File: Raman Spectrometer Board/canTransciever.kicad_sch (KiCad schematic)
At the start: 17 parts, among them SW1 SW_Push, SW2 SW_Push, U6 ATA6561, U7 ATA6561

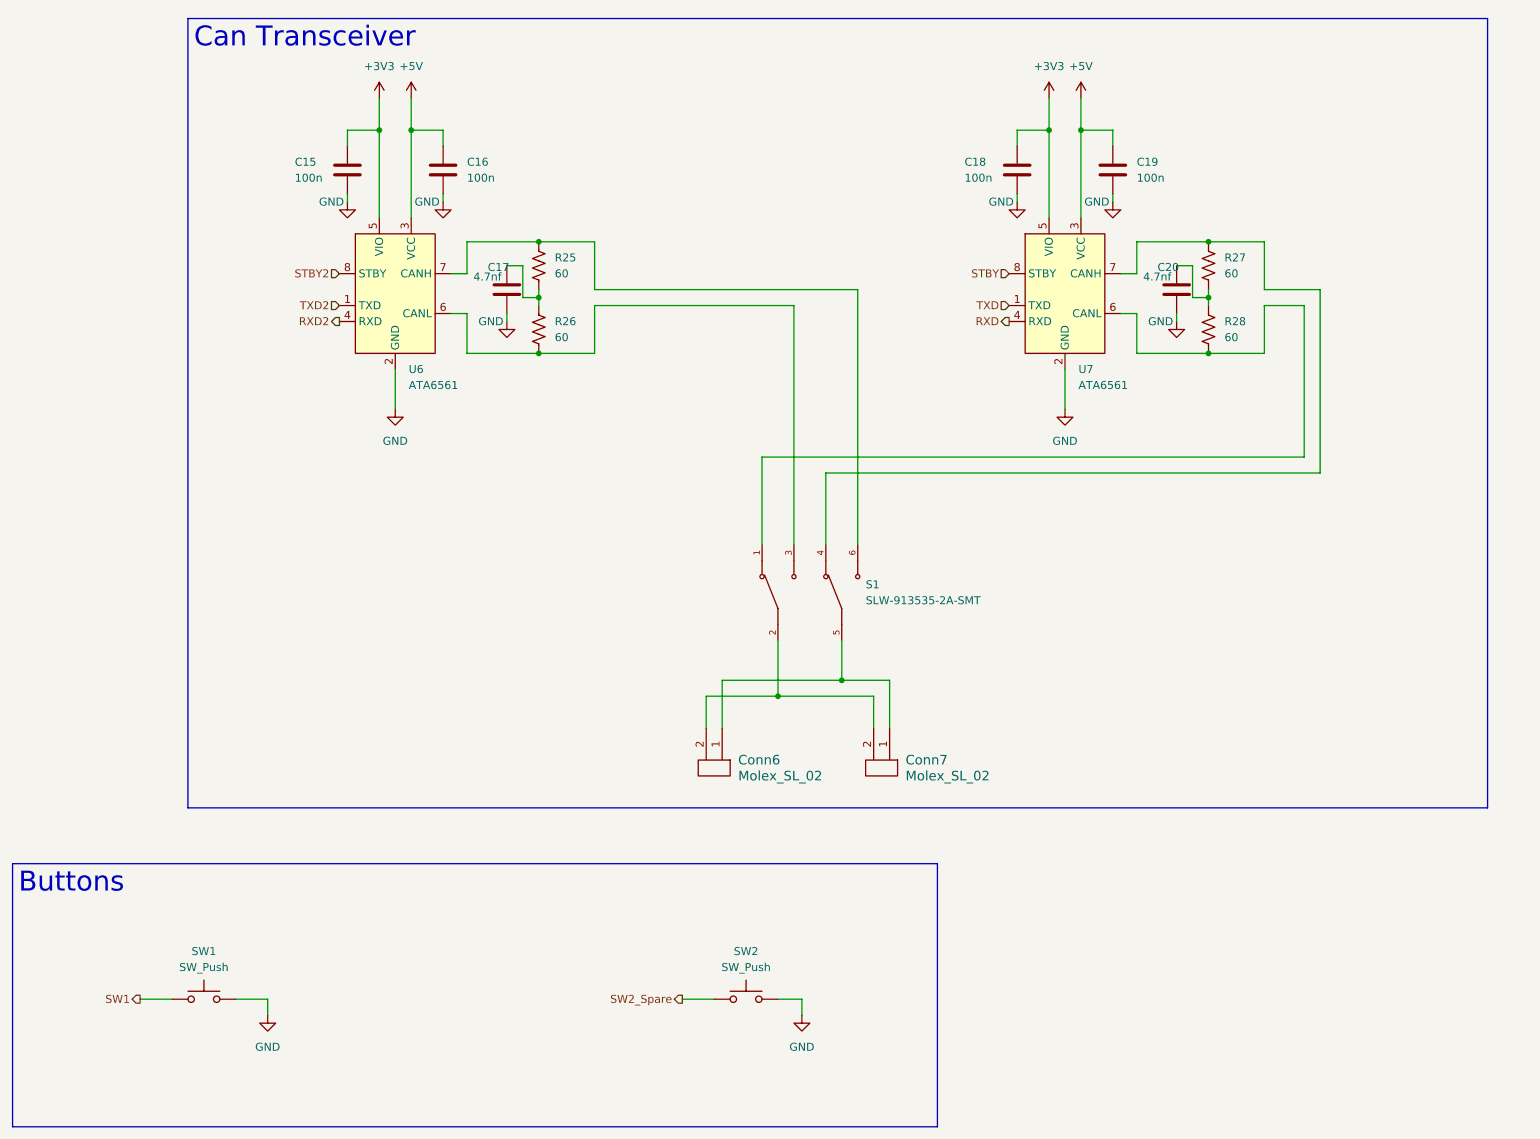
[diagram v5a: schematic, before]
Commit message: SCH fixes
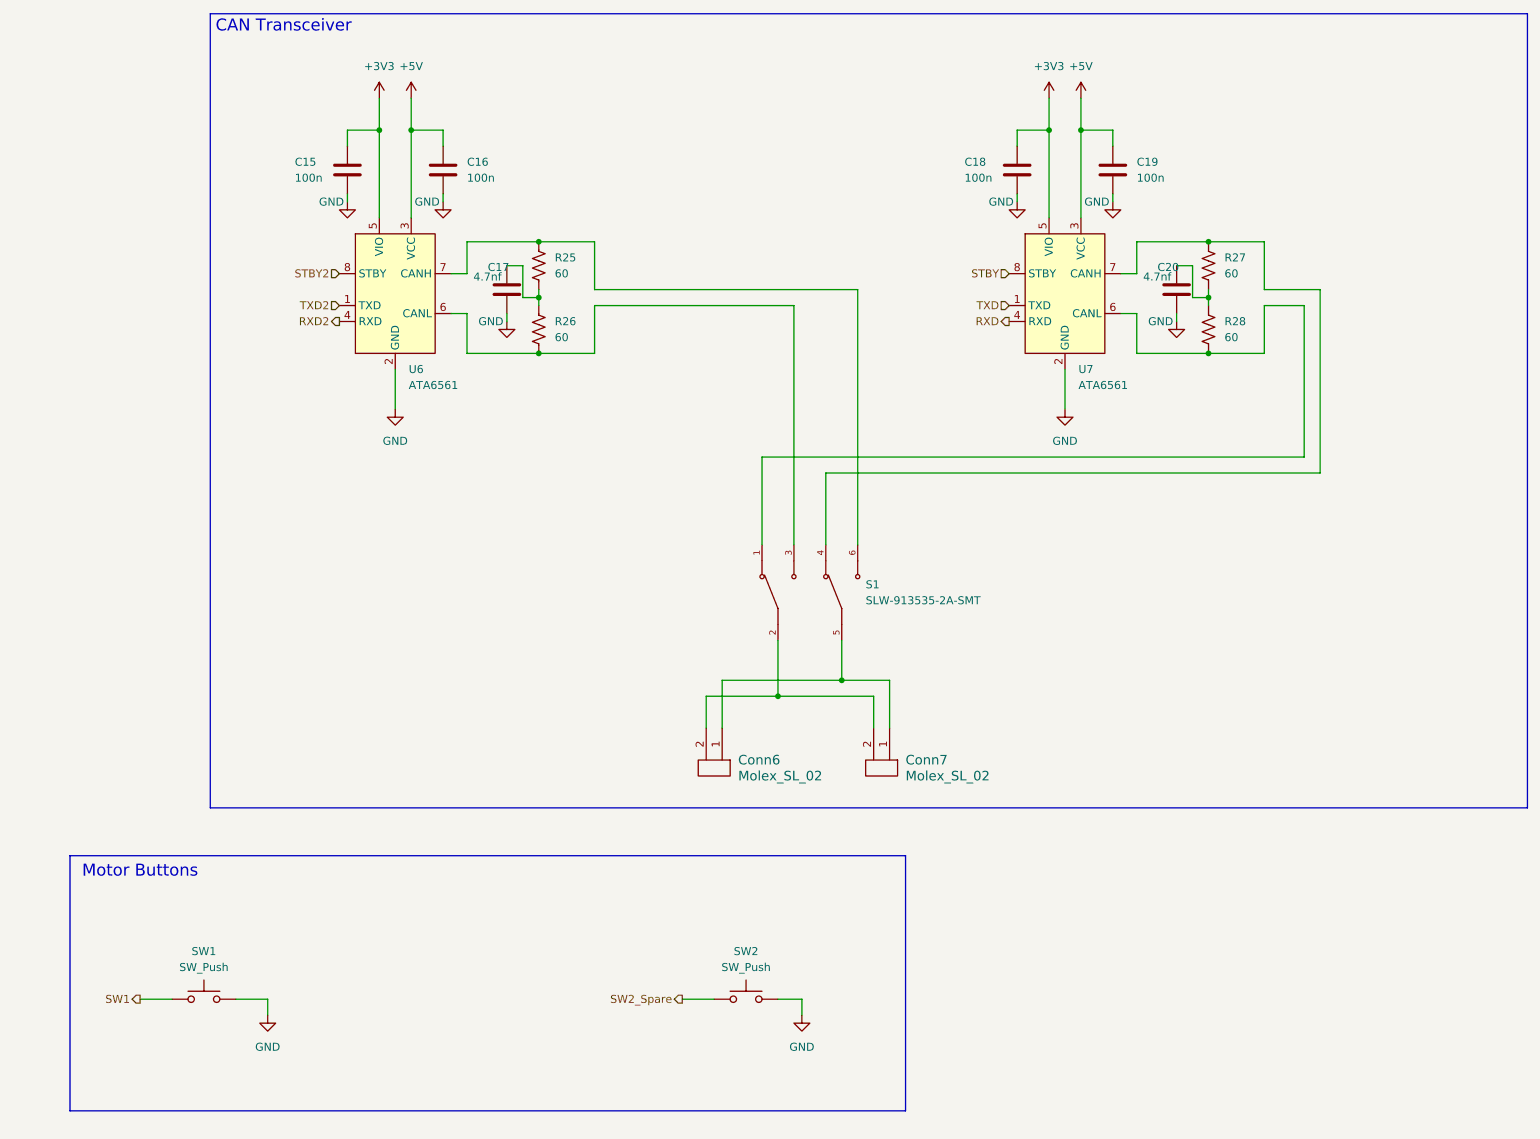
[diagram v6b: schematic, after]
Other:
- note added: "CAN Transceiver"
- note added: "Motor Buttons"
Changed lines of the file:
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@@
 	(generator_version "9.0")
 	(paper "A4")
-	(text_box "Can Transceiver"
-		(exclude_from_sim no)
-		(at 50.8 19.05 0)
-		(size 207.01 125.73)
-		(margins 0.9525 0.9525 0.9525 0.9525)
+	(rectangle
+		(start 54.356 18.288)
+		(end 264.16 144.78)
 		(stroke
 			(width 0)
-			(type solid)
+			(type default)
 		)
 		(fill
 			(type none)
 		)
-		(effects
-			(font
-				(size 3.175 3.175)
-			)
-			(justify left top)
-		)
 	)
-	(text_box "Buttons"
-		(exclude_from_sim no)
-		(at 22.86 153.67 0)
-		(size 147.32 41.91)
-		(margins 0.9525 0.9525 0.9525 0.9525)
+	(rectangle
+		(start 32.004 152.4)
+		(end 165.1 193.04)
 		(stroke
 			(width 0)
-			(type solid)
+			(type default)
 		)
 		(fill
 			(type none)
 		)
+	)
+	(text "CAN Transceiver"
+		(exclude_from_sim no)
+		(at 66.04 20.32 0)
 		(effects
 			(font
-				(size 3.175 3.175)
+				(size 1.905 1.905)
 			)
-			(justify left top)
 		)
 	)
+	(text "Motor Buttons"
+		(exclude_from_sim no)
+		(at 43.18 154.94 0)
+		(effects
+			(font
+				(size 1.905 1.905)
+			)
+		)
+	)

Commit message: Laser switch
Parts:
- removed C19: 100n, Capacitor_SMD:C_0603_1608Metric_Pad1.08x0.95mm_HandSolder, symbol Device:C
- removed C20: 4.7nf, Capacitor_SMD:C_0603_1608Metric_Pad1.08x0.95mm_HandSolder, symbol Device:C
- removed U6, U7: ATA6561, Package_SO:SOIC-8_3.9x4.9mm_P1.27mm, symbol MRDT_Devices:ATA6561
- added U6, U7: SN65HVD232, Package_SO:SOIC-8_3.9x4.9mm_P1.27mm, symbol Interface_CAN_LIN:SN65HVD232
- C18: value 100n -> 4.7nf
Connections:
- net +5V is gone; now on net +3V3: C16.1
- net +3V3: now also U6.3 (VCC), U7.3 (VCC); no longer C18.1
- net GND: now also U6.2 (GND), U7.2 (GND)
- net RXD: now also U7.4 (R)
- net RXD2: now also U6.4 (R)
- net TXD: now also U7.1 (D)
- net TXD2: now also U6.1 (D)
- net at R28.2, S1.1: now also U7.6 (CANL)
- net at R26.2, S1.3: now also U6.6 (CANL)
- net at R27.1, S1.4: now also U7.7 (CANH)
- net at R25.1, S1.6: now also U6.7 (CANH)
- net at R27.2, R28.1: now also C18.1
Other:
- moved on the sheet: C15
